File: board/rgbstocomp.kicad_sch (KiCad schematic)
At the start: 54 parts, among them U1 THS7316, U2 THS7316, U3 Opamp_Dual, U4 GS8743, U5 MIC5504-3.3YM5, Y1 TestPoint

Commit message: PCB design
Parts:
- removed R29: 2k73, symbol Device:R_Small
- removed U5: MIC5504-3.3YM5, Package_TO_SOT_SMD:SOT-23-5, symbol Regulator_Linear:MIC5504-3.3YM5
- added GND2, GND3: TestPoint, TestPoint:TestPoint_Pad_3.0x3.0mm, symbol Connector:TestPoint
- added U5: XC6206PxxxMR, Package_TO_SOT_SMD:SOT-23-3, symbol Regulator_Linear:XC6206PxxxMR
- C1, C10, C2, C3, C4, C5, C6, C7, C8, C9: footprint (none) -> Capacitor_SMD:C_0805_2012Metric_Pad1.18x1.45mm_HandSolder
- GND1, PB1, PR1, PWR5V1, PWRGND1, Y1: footprint (none) -> TestPoint:TestPoint_Pad_3.0x3.0mm
- JB1, JG1, JR1, JS1: footprint (none) -> footprints:156-0097-E
- R1, R10, R11, R12, R13, R14, R15, R16, R17, R18, R19, R2, R20, R21, R22, R23, R24, R25, R27, R28, R3, R4, R5, R6, R7, R8, R9: footprint (none) -> Resistor_SMD:R_0805_2012Metric_Pad1.20x1.40mm_HandSolder
- R26: value 2k20 -> 1k23; footprint (none) -> Resistor_SMD:R_0805_2012Metric_Pad1.20x1.40mm_HandSolder
- U1, U2, U3: footprint (none) -> Package_SO:SO-8_3.9x4.9mm_P1.27mm
- U4: footprint Package_TO_SOT_SMD:SOT-23-5 -> footprints:SOT-23-5
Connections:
- net +1V: no longer R27.1
- net +3V3: now also R27.1, U5.2 (VO)
- net +5V: now also U5.3 (VI)
- net GND: now also GND2.1, GND3.1, U5.1 (GND)
- net at R10.2, R11.1: now also U3.7; no longer U3.1
- net at R14.2, R15.2: now also U3.3 (+); no longer U3.5 (+)
- net at R16.2, R17.2, R18.2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: now also U3.2 (-); no longer U3.6 (-)
- net at R19.1, R20.2: now also U3.1; no longer U3.7
- net at R10.1, R7.2, R8.2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: now also U3.6 (-); no longer U3.2 (-)
- net at R12.2, R13.2: now also U3.5 (+); no longer U3.3 (+)
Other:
- moved on the sheet: C7, GND1, PB1, PR1, R10, R11, R12, R13, R14, R15, R16, R17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

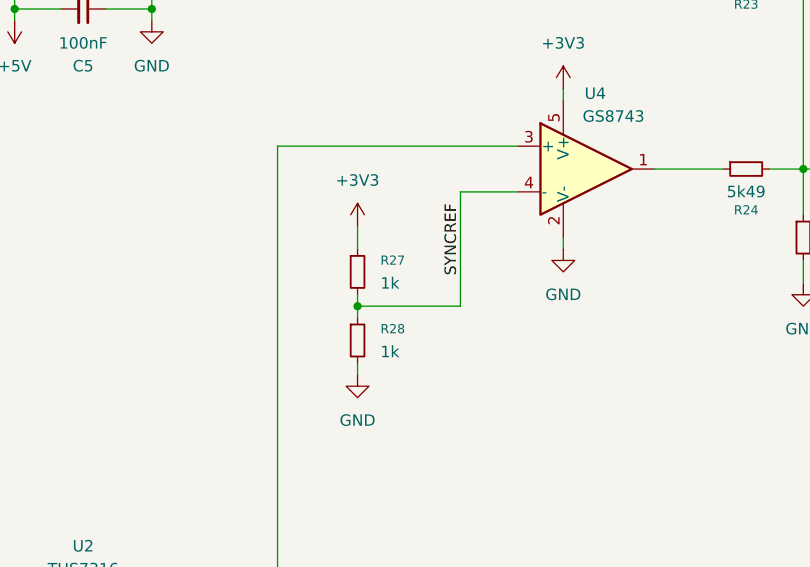
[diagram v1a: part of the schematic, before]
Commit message: Fix CSYNC detection threashold
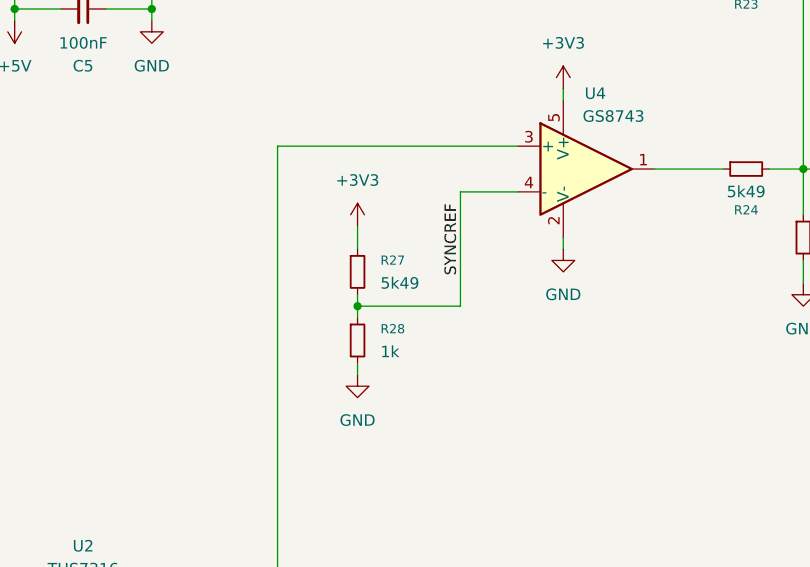
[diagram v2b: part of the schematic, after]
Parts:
- R27: value 1k -> 5k49
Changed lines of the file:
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@@
 			)
 		)
-		(property "Value" "1k"
+		(property "Value" "5k49"
 			(at 109.22 85.0899 0)
 			(effects

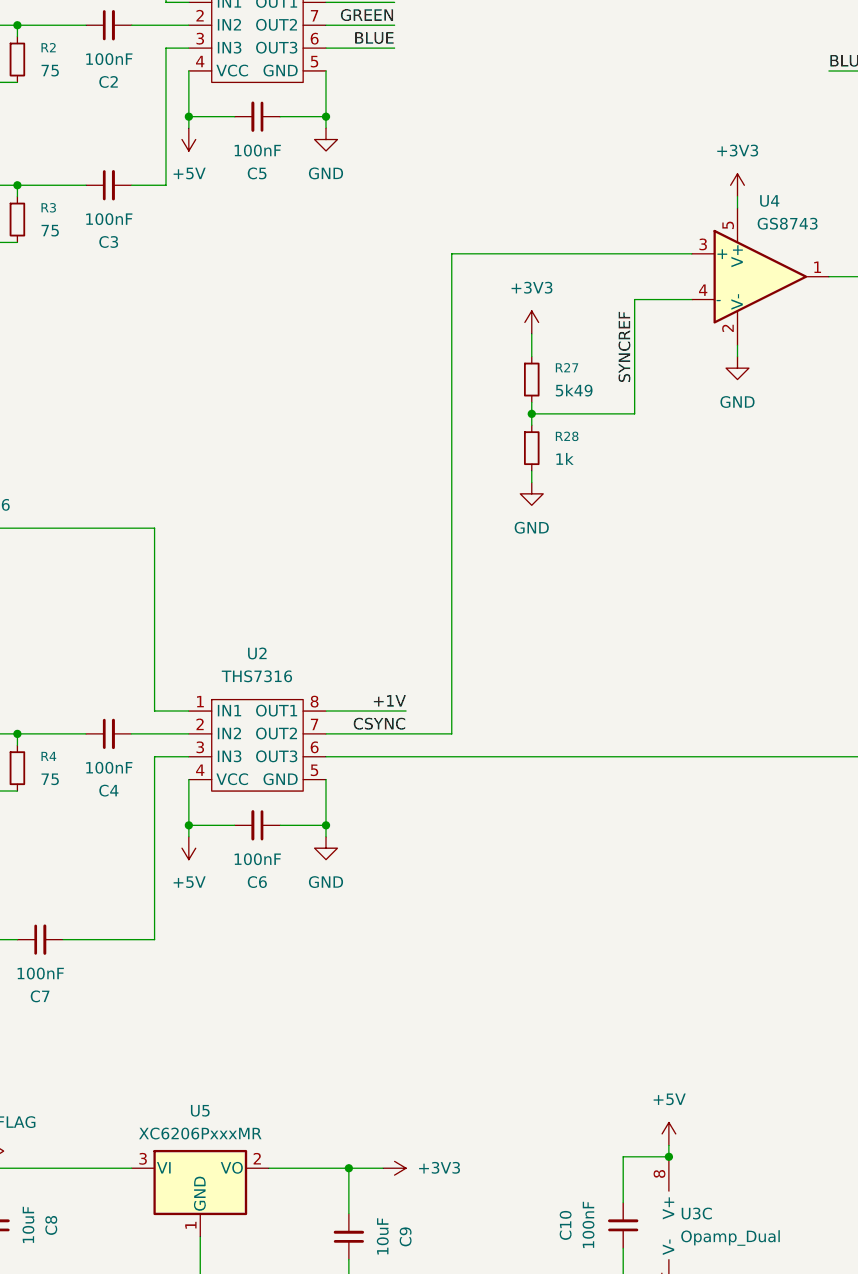
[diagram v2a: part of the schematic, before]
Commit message: Supply ICs with 3.3V instead of with 5V. Add documentation.
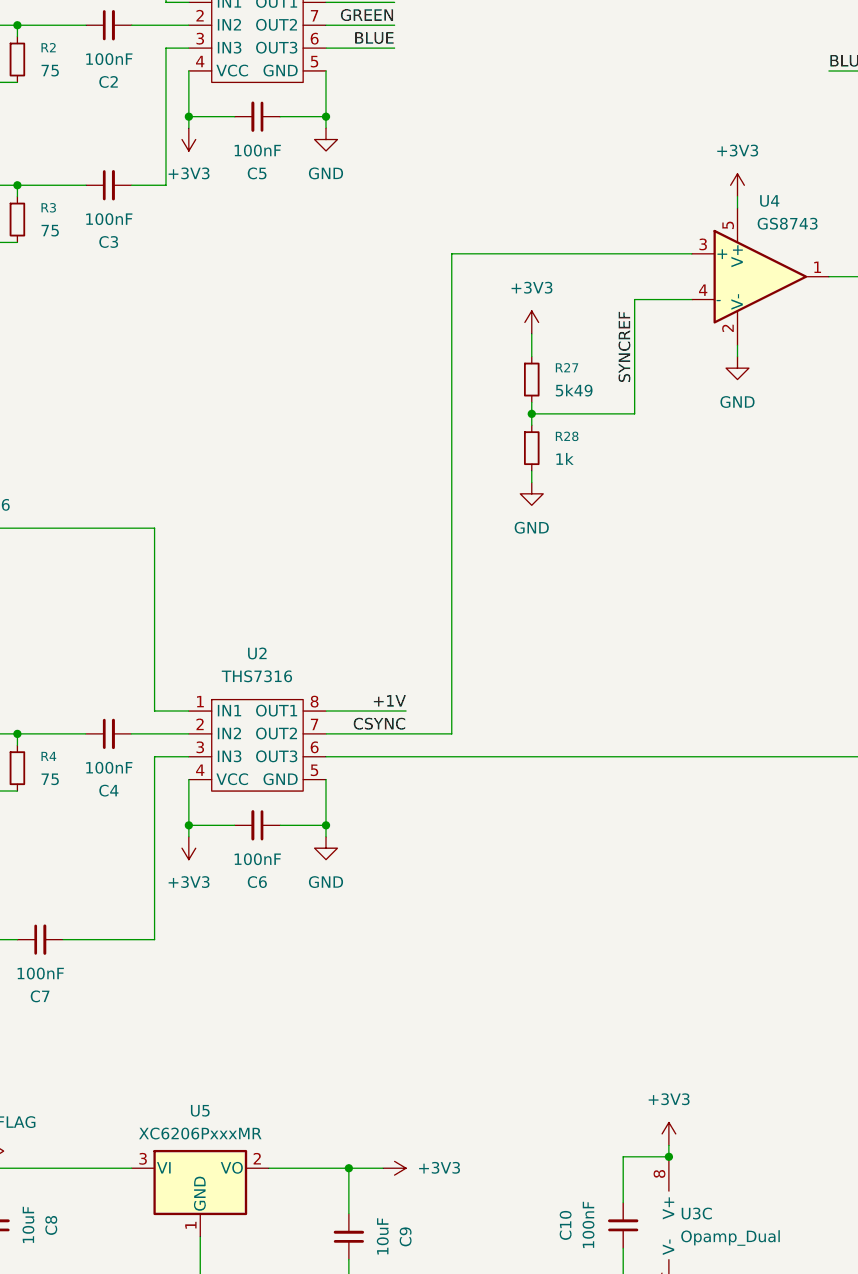
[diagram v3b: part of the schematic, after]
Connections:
- net +3V3: now also C10.2, C5.2, C6.2, U1.4 (VCC), U2.4 (VCC), U3.8 (V+)
- net +5V: no longer C10.2, C5.2, C6.2, U1.4 (VCC), U2.4 (VCC), U3.8 (V+)
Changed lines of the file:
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@@
 	)
 	(symbol
-		(lib_id "power:+5V")
-		(at 68.58 55.88 180)
-		(unit 1)
-		(exclude_from_sim no)
-		(in_bom yes)
-		(on_board yes)
-		(dnp no)
-		(fields_autoplaced yes)
-		(property "Reference" "#PWR08"
-			(at 68.58 52.07 0)
-			(effects
-				(font
-					(size 1.27 1.27)
-				)
-				(hide yes)
-			)
-		)
-		(property "Value" "+5V"
-			(at 68.58 60.96 0)
-			(effects
-				(font
-					(size 1.27 1.27)
-				)
-			)
-		)
-		(property "Footprint" ""
-			(at 68.58 55.88 0)
-			(effects
-				(font
-					(size 1.27 1.27)
-				)
-				(hide yes)
-			)
-		)
-		(property "Datasheet" ""
-			(at 68.58 55.88 0)
-			(effects
-				(font
-					(size 1.27 1.27)
-				)
-				(hide yes)
-			)
-		)
-		(property "Description" "Power symbol creates a global label with name \"+5V\""
-			(at 68.58 55.88 0)
-			(effects
-				(font
-					(size 1.27 1.27)
-				)
-				(hide yes)
-			)
-		)
-		(pin "1"
-		)
-		(instances
-			(project ""
-				(path "/ac4b55fc-83c7-4cff-900d-6958ba79f0ee"
-					(reference "#PWR08")
-					(unit 1)
-				)
-			)
-		)
-	)
-	(symbol
 		(lib_id "Device:R_Small")
 		(at 106.68 91.44 0)
@@
 	)
 	(symbol
+		(lib_id "power:+3V3")
+		(at 121.92 168.91 0)
+		(unit 1)
+		(exclude_from_sim no)
+		(in_bom yes)
+		(on_board yes)
+		(dnp no)
+		(fields_autoplaced yes)
+		(property "Reference" "#PWR020"
+			(at 121.92 172.72 0)
+			(effects
+				(font
+					(size 1.27 1.27)
+				)
+				(hide yes)
+			)
+		)
+		(property "Value" "+3V3"
+			(at 121.92 163.83 0)
+			(effects
+				(font
+					(size 1.27 1.27)
+				)
+			)
+		)
+		(property "Footprint" ""
+			(at 121.92 168.91 0)
+			(effects
+				(font
+					(size 1.27 1.27)
+				)
+				(hide yes)
+			)
+		)
+		(property "Datasheet" ""
+			(at 121.92 168.91 0)
+			(effects
+				(font
+					(size 1.27 1.27)
+				)
+				(hide yes)
+			)
+		)
+		(property "Description" "Power symbol creates a global label with name \"+3V3\""
+			(at 121.92 168.91 0)
+			(effects
+				(font
+					(size 1.27 1.27)
+				)
+				(hide yes)
+			)
+		)
+		(pin "1"
+		)
+		(instances
+			(project "rgbstocomp"
+				(path "/ac4b55fc-83c7-4cff-900d-6958ba79f0ee"
+					(reference "#PWR020")
+					(unit 1)
+				)
+			)
+		)
+	)
+	(symbol
 		(lib_id "Device:R_Small")
 		(at 219.71 102.87 90)
@@
 	)
 	(symbol
-		(lib_id "power:+5V")
-		(at 68.58 134.62 180)
-		(unit 1)
-		(exclude_from_sim no)
-		(in_bom yes)
-		(on_board yes)
-		(dnp no)
-		(fields_autoplaced yes)
-		(property "Reference" "#PWR07"
-			(at 68.58 130.81 0)
-			(effects
-				(font
-					(size 1.27 1.27)
-				)
-				(hide yes)
-			)
-		)
-		(property "Value" "+5V"
-			(at 68.58 139.7 0)
-			(effects
-				(font
-					(size 1.27 1.27)
-				)
-			)
-		)
-		(property "Footprint" ""
-			(at 68.58 134.62 0)
-			(effects
-				(font
-					(size 1.27 1.27)
-				)
-				(hide yes)
-			)
-		)
-		(property "Datasheet" ""
-			(at 68.58 134.62 0)
-			(effects
-				(font
-					(size 1.27 1.27)
-				)
-				(hide yes)
-			)
-		)
-		(property "Description" "Power symbol creates a global label with name \"+5V\""
-			(at 68.58 134.62 0)
-			(effects
-				(font
-					(size 1.27 1.27)
-				)
-				(hide yes)
-			)
-		)
-		(pin "1"
-		)
-		(instances
-			(project ""
-				(path "/ac4b55fc-83c7-4cff-900d-6958ba79f0ee"
-					(reference "#PWR07")
-					(unit 1)
-				)
-			)
-		)
-	)
-	(symbol
 		(lib_id "Device:R_Small")
 		(at 106.68 83.82 0)
@@
 	)
 	(symbol
+		(lib_id "power:+3V3")
+		(at 68.58 134.62 180)
+		(unit 1)
+		(exclude_from_sim no)
+		(in_bom yes)
+		(on_board yes)
+		(dnp no)
+		(fields_autoplaced yes)
+		(property "Reference" "#PWR07"
+			(at 68.58 130.81 0)
+			(effects
+				(font
+					(size 1.27 1.27)
+				)
+				(hide yes)
+			)
+		)
+		(property "Value" "+3V3"
+			(at 68.58 139.7 0)
+			(effects
+				(font
+					(size 1.27 1.27)
+				)
+			)
+		)
+		(property "Footprint" ""
+			(at 68.58 134.62 0)
+			(effects
+				(font
+					(size 1.27 1.27)
+				)
+				(hide yes)
+			)
+		)
+		(property "Datasheet" ""
+			(at 68.58 134.62 0)
+			(effects
+				(font
+					(size 1.27 1.27)
+				)
+				(hide yes)
+			)
+		)
+		(property "Description" "Power symbol creates a global label with name \"+3V3\""
+			(at 68.58 134.62 0)
+			(effects
+				(font
+					(size 1.27 1.27)
+				)
+				(hide yes)
+			)
+		)
+		(pin "1"
+		)
+		(instances
+			(project "rgbstocomp"
+				(path "/ac4b55fc-83c7-4cff-900d-6958ba79f0ee"
+					(reference "#PWR07")
+					(unit 1)
+				)
+			)
+		)
+	)
+	(symbol
 		(lib_id "Device:R_Small")
 		(at 204.47 111.76 90)
@@
 	)
 	(symbol
+		(lib_id "power:+3V3")
+		(at 68.58 55.88 180)
+		(unit 1)
+		(exclude_from_sim no)
+		(in_bom yes)
+		(on_board yes)
+		(dnp no)
+		(fields_autoplaced yes)
+		(property "Reference" "#PWR08"
+			(at 68.58 52.07 0)
+			(effects
+				(font
+					(size 1.27 1.27)
+				)
+				(hide yes)
+			)
+		)
+		(property "Value" "+3V3"
+			(at 68.58 60.96 0)
+			(effects
+				(font
+					(size 1.27 1.27)
+				)
+			)
+		)
+		(property "Footprint" ""
+			(at 68.58 55.88 0)
+			(effects
+				(font
+					(size 1.27 1.27)
+				)
+				(hide yes)
+			)
+		)
+		(property "Datasheet" ""
+			(at 68.58 55.88 0)
+			(effects
+				(font
+					(size 1.27 1.27)
+				)
+				(hide yes)
+			)
+		)
+		(property "Description" "Power symbol creates a global label with name \"+3V3\""
+			(at 68.58 55.88 0)
+			(effects
+				(font
+					(size 1.27 1.27)
+				)
+				(hide yes)
+			)
+		)
+		(pin "1"
+		)
+		(instances
+			(project "rgbstocomp"
+				(path "/ac4b55fc-83c7-4cff-900d-6958ba79f0ee"
+					(reference "#PWR08")
+					(unit 1)
+				)
+			)
+		)
+	)
+	(symbol
 		(lib_id "Device:R_Small")
 		(at 234.95 125.73 90)
@@
 					(unit 1)
 				)
-			)
-		)
-	)
-	(symbol
-		(lib_id "power:+5V")
-		(at 121.92 168.91 0)
-		(unit 1)
-		(exclude_from_sim no)
-		(in_bom yes)
-		(on_board yes)
-		(dnp no)
-		(fields_autoplaced yes)
-		(property "Reference" "#PWR020"
-			(at 121.92 172.72 0)
-			(effects
-				(font
-					(size 1.27 1.27)
-				)
-				(hide yes)
-			)
-		)
-		(property "Value" "+5V"
-			(at 121.92 163.83 0)
-			(effects
-				(font
-					(size 1.27 1.27)
-				)
-			)
-		)
-		(property "Footprint" ""
-			(at 121.92 168.91 0)
-			(effects
-				(font
-					(size 1.27 1.27)
-				)
-				(hide yes)
-			)
-		)
-		(property "Datasheet" ""
-			(at 121.92 168.91 0)
-			(effects
-				(font
-					(size 1.27 1.27)
-				)
-				(hide yes)
-			)
-		)
-		(property "Description" "Power symbol creates a global label with name \"+5V\""
-			(at 121.92 168.91 0)
-			(effects
-				(font
-					(size 1.27 1.27)
-				)
-				(hide yes)
-			)
-		)
-		(pin "1"
-		)
-		(instances
-			(project "rgbstocomp"
-				(path "/ac4b55fc-83c7-4cff-900d-6958ba79f0ee"
-					(reference "#PWR020")
-					(unit 1)
-				)

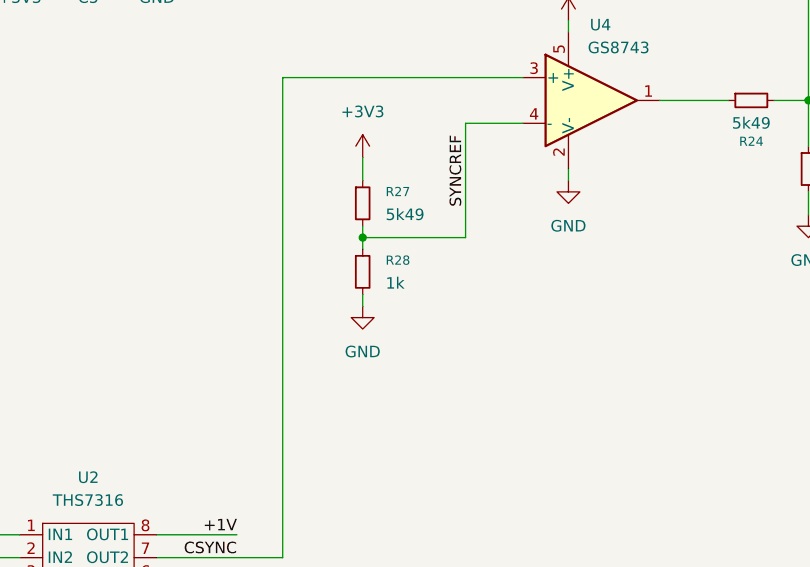
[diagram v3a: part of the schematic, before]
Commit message: Change resistor to create the csync reference voltage
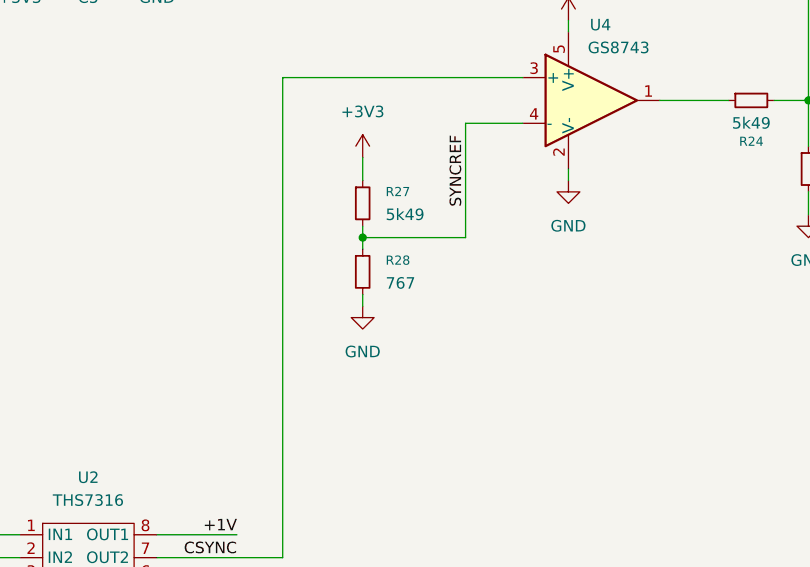
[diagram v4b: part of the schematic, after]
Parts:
- R28: value 1k -> 767
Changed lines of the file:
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@@
 			)
 		)
-		(property "Value" "1k"
+		(property "Value" "767"
 			(at 109.22 92.7099 0)
 			(effects
